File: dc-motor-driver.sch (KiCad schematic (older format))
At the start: 26 parts, among them J1 Conn_01x03, J10 Right, J11 RL, J12 RR, J2 MPU, J3 BAT, J4 Conn_01x03, J5 Power, J6 Left, J7 Conn_01x03, J8 FL, J9 FR, Q1 IRF7303, Q2 IRF7303

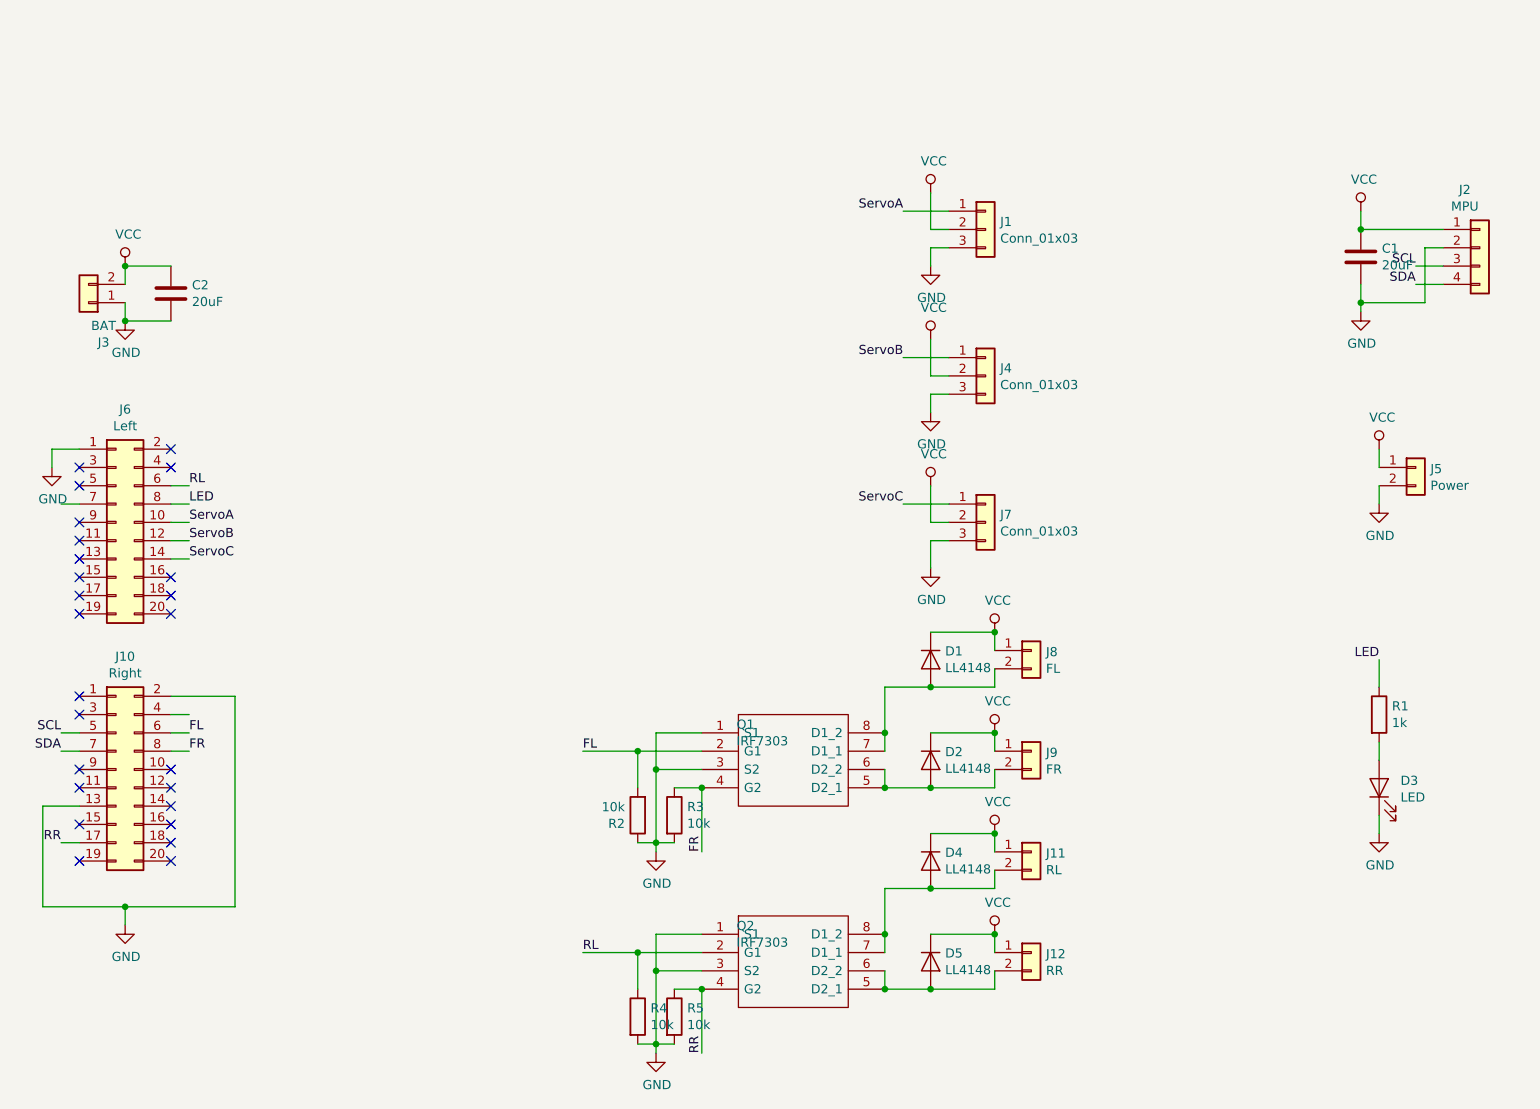
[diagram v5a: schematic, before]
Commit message: Changed the power source for the MPU.
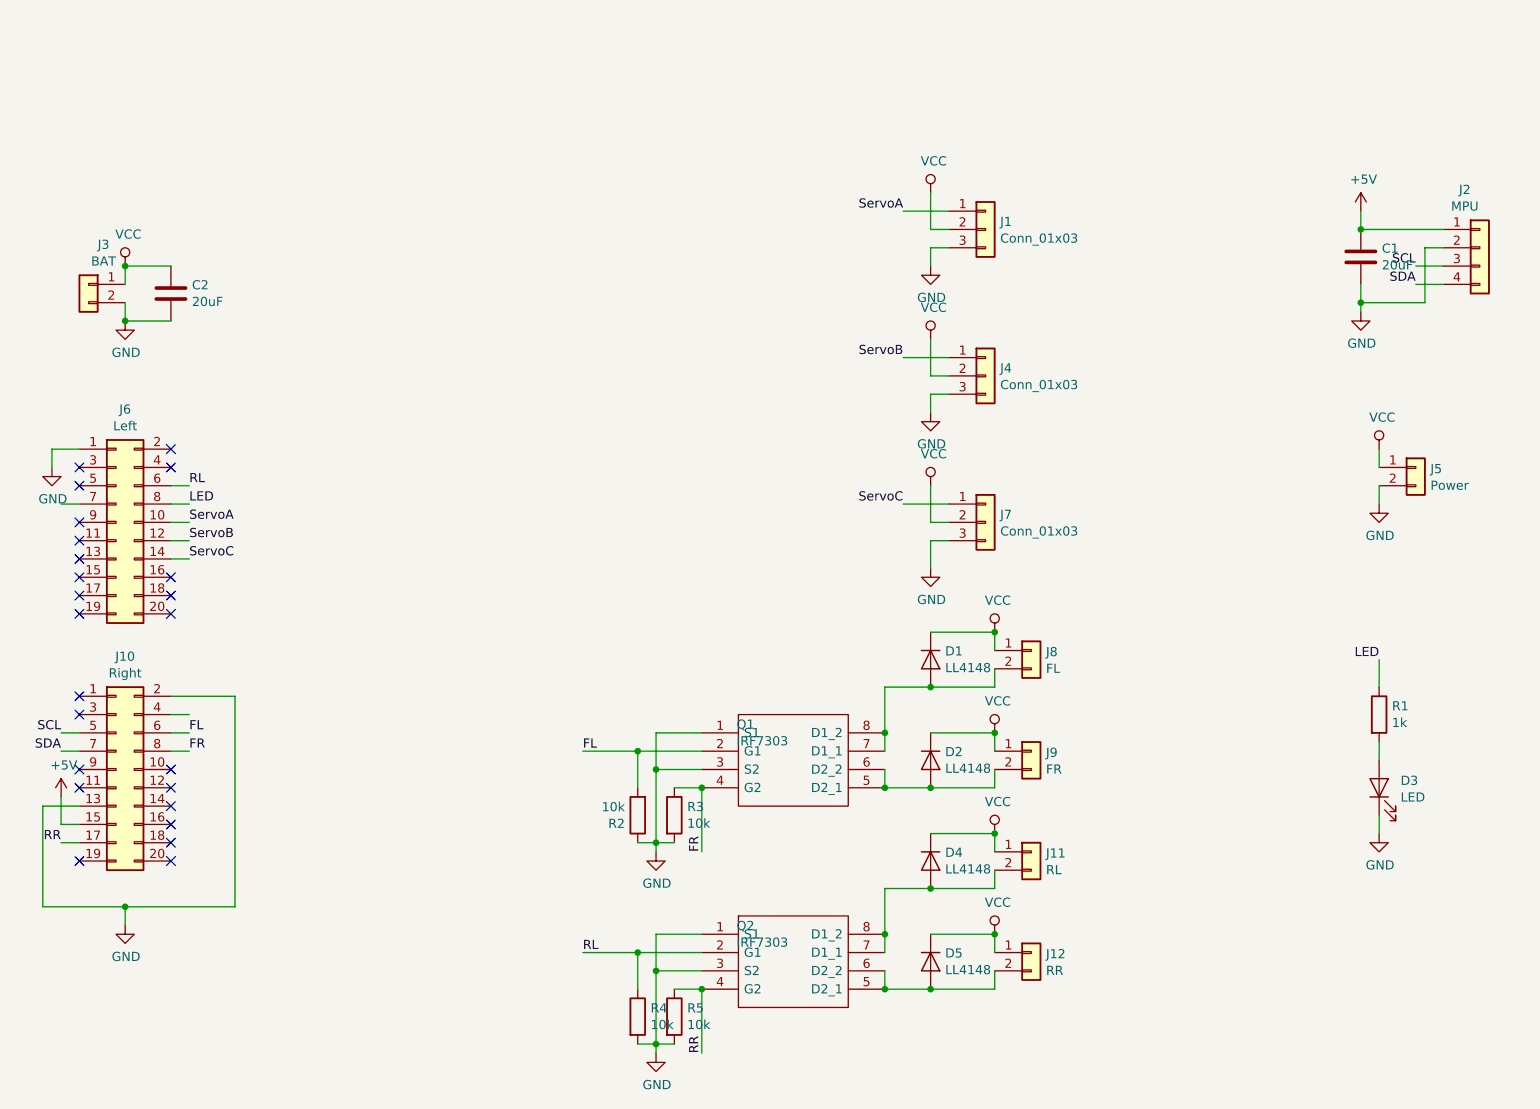
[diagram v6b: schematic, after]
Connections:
- net GND: now also J3.2 (Pin_2); no longer J3.1 (Pin_1)
- net VCC: now also J3.1 (Pin_1); no longer C1.1, J2.1 (Pin_1), J3.2 (Pin_2)
- net +5V: now reaches J10.15 (Pin_15)
- net +5V: now also C1.1, J2.1 (Pin_1)
- no-connect marks 25 -> 24
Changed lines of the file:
@@
 L Connector_Generic:Conn_01x02 J3
 U 1 1 5DB9E165
-P 1950 2250
-F 0 "J3" H 1868 2467 50  0000 C CNN
-F 1 "BAT" H 1868 2376 50  0000 C CNN
-F 2 "Connector_JST:JST_XH_S2B-XH-A-1_1x02_P2.50mm_Horizontal" H 1950 2250 50  0001 C CNN
-F 3 "~" H 1950 2250 50  0001 C CNN
-	1    1950 2250
-	-1   0    0    1
+P 1950 2150
+F 0 "J3" H 1868 2367 50  0000 C CNN
+F 1 "BAT" H 1868 2276 50  0000 C CNN
+F 2 "Connector_JST:JST_XH_S2B-XH-A-1_1x02_P2.50mm_Horizontal" H 1950 2150 50  0001 C CNN
+F 3 "~" H 1950 2150 50  0001 C CNN
+	1    1950 2150
+	-1   0    0    -1
 $EndComp
 Wire Wire Line
@@
 ServoA
 $Comp
-L power:VCC #PWR02
-U 1 1 5E022BA3
-P 8900 1750
-F 0 "#PWR02" H 8900 1600 50  0001 C CNN
-F 1 "VCC" H 8917 1923 50  0000 C CNN
-F 2 "" H 8900 1750 50  0001 C CNN
-F 3 "" H 8900 1750 50  0001 C CNN
-	1    8900 1750
-	1    0    0    -1
-$EndComp
-$Comp
 L power:GND #PWR010
 U 1 1 5E023207
@@
 Wire Wire Line
 	8900 1850 9350 1850
-Wire Wire Line
-	8900 1850 8900 1750
 Connection ~ 8900 1850
 $Comp
@@
 NoConn ~ 2400 5300
 NoConn ~ 1900 5300
-NoConn ~ 1900 5100
 NoConn ~ 1900 4900
 NoConn ~ 1900 4800
@@
 NoConn ~ 1900 3150
 NoConn ~ 2400 3150
-NoConn ~ 2400 3750
 NoConn ~ 2400 3850
 NoConn ~ 2400 3950
@@
 Wire Wire Line
 	2400 3650 2500 3650
+Wire Wire Line
+	8900 1850 8900 1750
+$Comp
+L power:+5V #PWR0102
+U 1 1 5DF306DD
+P 1800 4950
+F 0 "#PWR0102" H 1800 4800 50  0001 C CNN
+F 1 "+5V" H 1815 5123 50  0000 C CNN
+F 2 "" H 1800 4950 50  0001 C CNN
+F 3 "" H 1800 4950 50  0001 C CNN
+	1    1800 4950
+	1    0    0    -1
+$EndComp
+$Comp
+L power:+5V #PWR0103
+U 1 1 5DF30C57
+P 8900 1750
+F 0 "#PWR0103" H 8900 1600 50  0001 C CNN
+F 1 "+5V" H 8915 1923 50  0000 C CNN
+F 2 "" H 8900 1750 50  0001 C CNN
+F 3 "" H 8900 1750 50  0001 C CNN
+	1    8900 1750
+	1    0    0    -1
+$EndComp
+NoConn ~ 2400 3750
+Wire Wire Line
+	1900 5100 1800 5100
+Wire Wire Line
+	1800 5100 1800 4950
 $EndSCHEMATC

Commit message: Removed an unused wire.
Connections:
- no-connect marks 24 -> 25
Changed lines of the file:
@@
 Text Label 2500 3350 0    50   ~ 0
 LED
-Wire Wire Line
-	2400 4500 2500 4500
 NoConn ~ 2400 4800
 NoConn ~ 2400 4900
@@
 Wire Wire Line
 	1800 5100 1800 4950
+NoConn ~ 2400 4500
 $EndSCHEMATC
